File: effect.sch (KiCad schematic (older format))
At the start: 32 parts, among them Q1 2N7000, Q2 2N7000, U5 TL072, U6 TL072

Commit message: Fix a few values
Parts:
- removed C13: 47u, symbol Device:CP
- added C?: 47u, symbol Device:C
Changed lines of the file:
@@
-$EndComp
-$Comp
-L Device:CP C13
-U 1 1 60D39B10
-P 8650 1650
-F 0 "C13" H 8768 1696 50  0000 L CNN
-F 1 "47u" H 8768 1605 50  0000 L CNN
-F 2 "" H 8688 1500 50  0001 C CNN
-F 3 "~" H 8650 1650 50  0001 C CNN
-	1    8650 1650
-	1    0    0    -1
 $EndComp
 $Comp
@@
 Wire Wire Line
 	2400 1750 2400 2450
+$Comp
+L Device:C C?
+U 1 1 60E2FADA
+P 8650 1650
+F 0 "C?" H 8765 1696 50  0000 L CNN
+F 1 "47u" H 8765 1605 50  0000 L CNN
+F 2 "" H 8688 1500 50  0001 C CNN
+F 3 "~" H 8650 1650 50  0001 C CNN
+	1    8650 1650
+	1    0    0    -1
+$EndComp
 $EndSCHEMATC

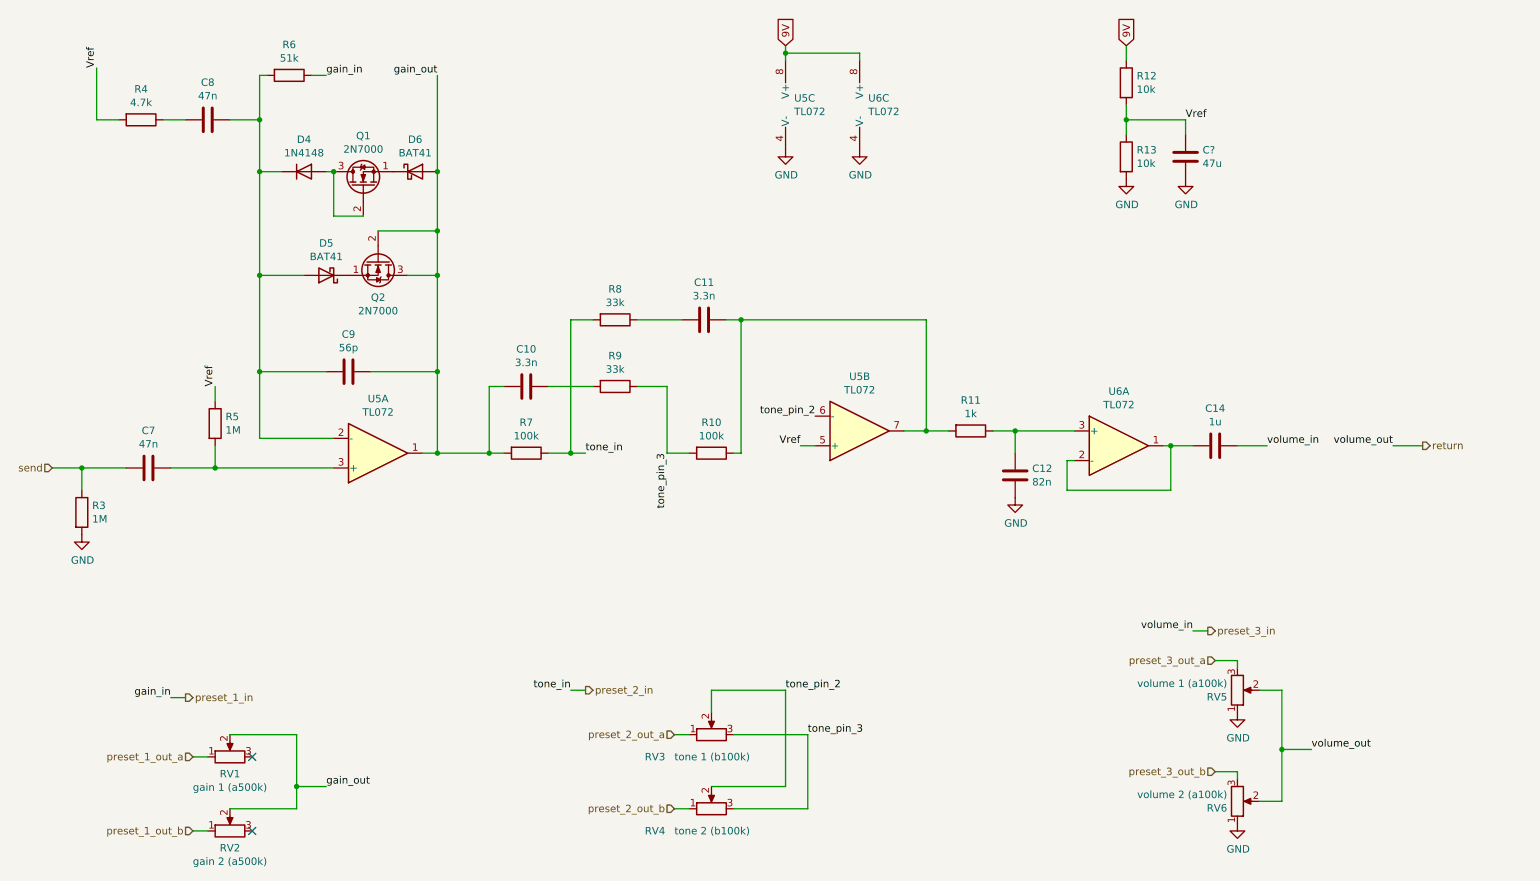
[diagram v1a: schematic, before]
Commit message: Now with an input buffer to preserve phase
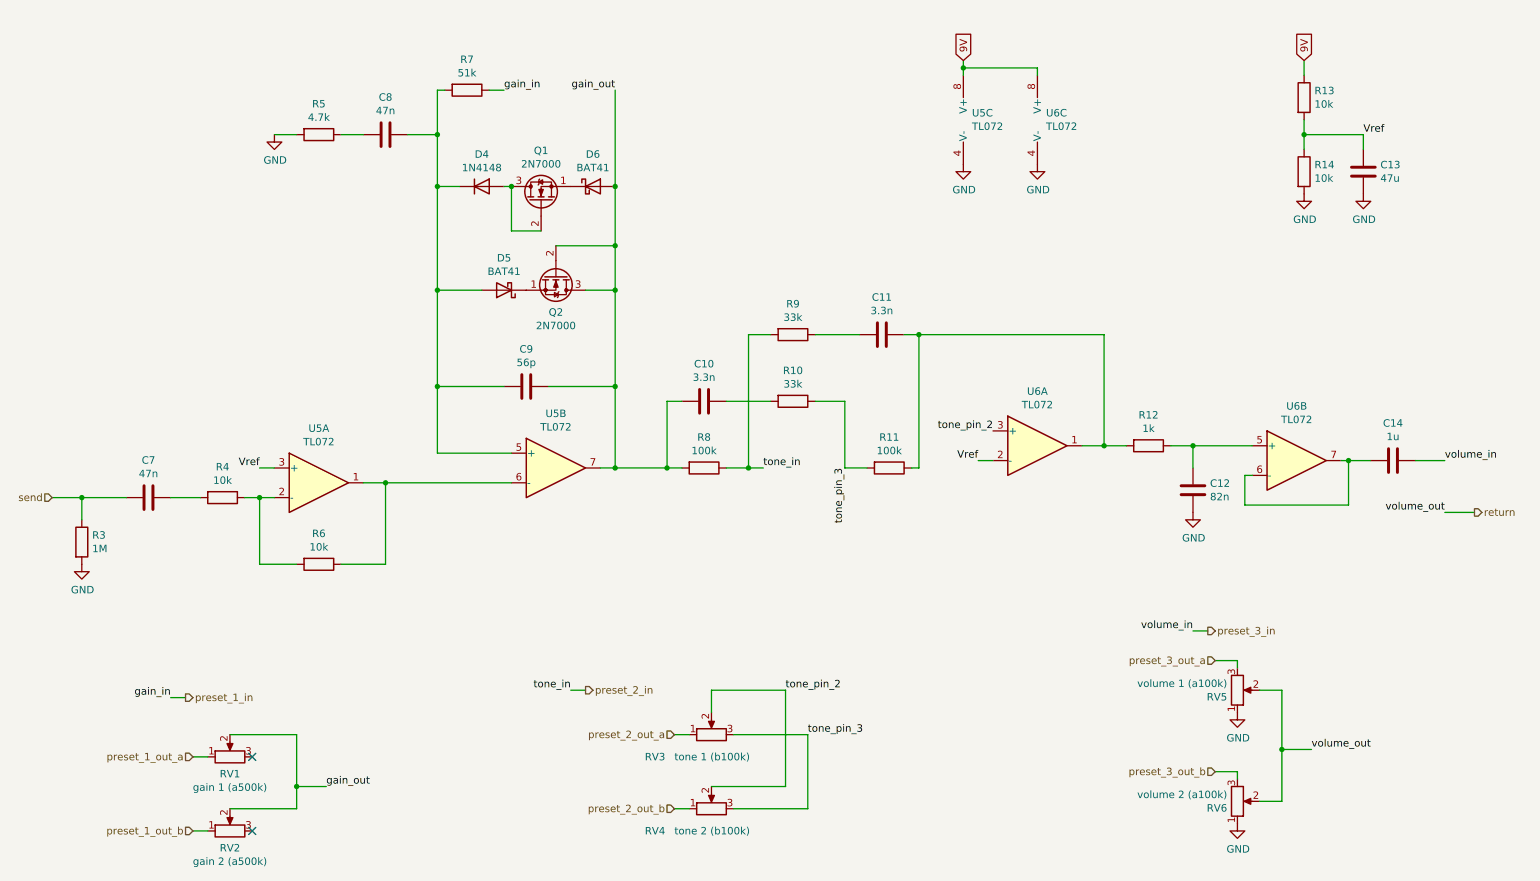
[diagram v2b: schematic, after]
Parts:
- removed R5: 1M, symbol Device:R
- added R4, R6: 10k, symbol Device:R
- added unit 2 of U6
- gave numbers to parts that had none: 1
- renumbered R9 to R10, R10 to R11, R11 to R12, R12 to R13, R13 to R14, R4 to R5, R6 to R7, R7 to R8, R8 to R9
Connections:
- net GND: now also R5.2
- net Vref: now also U5.3 (+), U6.2 (-); no longer R5.2, U5.5 (+)
- net gain_out: now also U5.7; no longer U5.1
- net tone_pin_2: now also U6.3 (+); no longer U5.6 (-)
- net at C8.1, C9.2, D4.1 (K)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: now also U5.5 (+); no longer U5.2 (-)
- net at C7.1: now also R4.2; no longer U5.3 (+)
- net at C11.1, R11.1, R12.2: now also U6.1; no longer U5.7
- net at C12.2, R12.1: now also U6.5 (+); no longer U6.3 (+)
- new net: C14.2, U6.6 (-), U6.7
- new net: R6.1, U5.1, U5.6 (-)
- new net: R4.1, R6.2, U5.2 (-)
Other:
- moved on the sheet: C10, C11, C12, C13, C14, C7, C8, C9, D4, D5, D6, Q1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

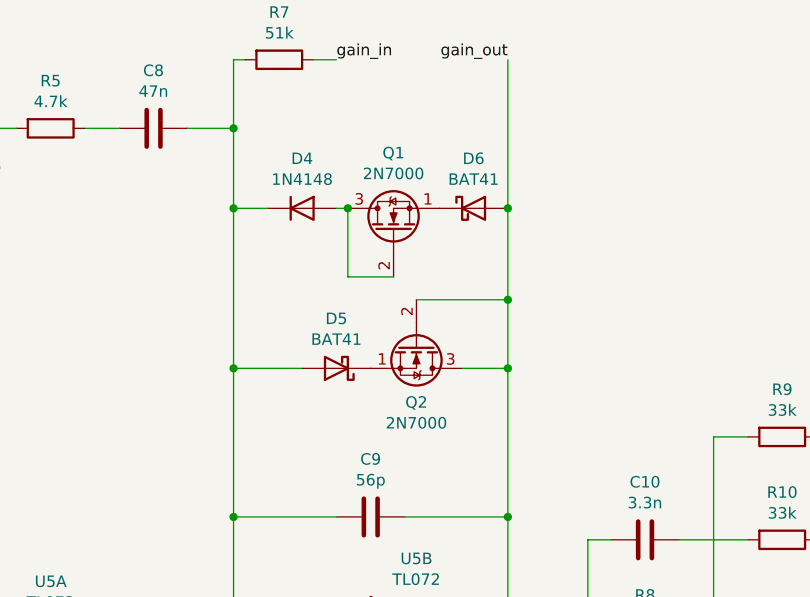
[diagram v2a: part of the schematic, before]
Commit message: Add resistor footprints/part numbers
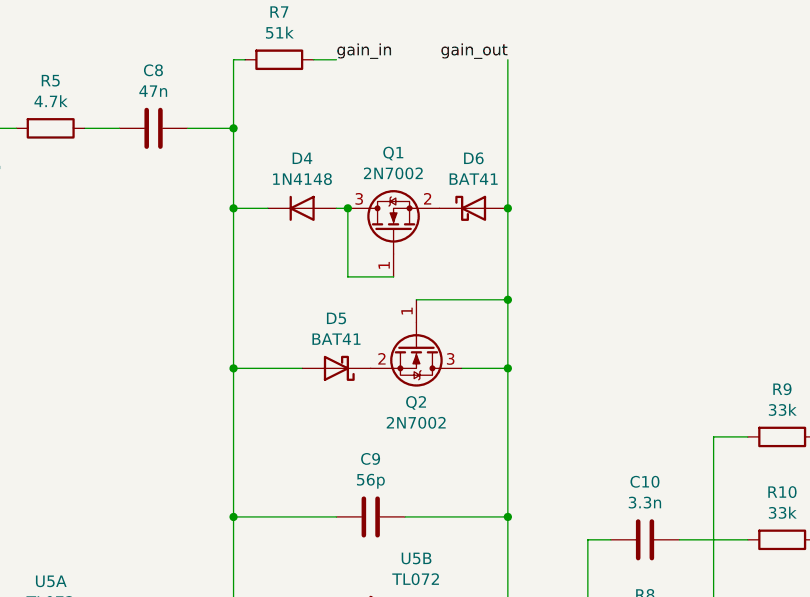
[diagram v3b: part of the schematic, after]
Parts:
- removed Q1, Q2: 2N7000, Package_TO_SOT_THT:TO-92_Inline, symbol Transistor_FET:2N7000
- added Q1, Q2: 2N7002, Package_TO_SOT_SMD:SOT-23, symbol Transistor_FET:2N7002
- R10, R9: footprint (none) -> Resistor_SMD:R_0603_1608Metric; LCSC (none) -> C4216
- R11, R8: footprint (none) -> Resistor_SMD:R_0603_1608Metric; LCSC (none) -> C25803
- R12: footprint (none) -> Resistor_SMD:R_0603_1608Metric; LCSC (none) -> C21190
- R13, R14, R4, R6: footprint (none) -> Resistor_SMD:R_0603_1608Metric; LCSC (none) -> C25804
- R3: footprint (none) -> Resistor_SMD:R_0603_1608Metric; LCSC (none) -> C22935
- R5: footprint (none) -> Resistor_SMD:R_0603_1608Metric; LCSC (none) -> C23162
- R7: footprint (none) -> Resistor_SMD:R_0603_1608Metric; LCSC (none) -> C23196
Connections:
- net gain_out: now also Q2.1 (G), Q2.3 (D)
- net at D5.1 (K): now also Q2.2 (S)
- net at D6.1 (K): now also Q1.2 (S)
- net at D4.2 (A): now also Q1.1 (G), Q1.3 (D)
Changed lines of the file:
@@
 F 0 "R7" V 3593 1200 50  0000 C CNN
 F 1 "51k" V 3684 1200 50  0000 C CNN
-F 2 "" V 3730 1200 50  0001 C CNN
+F 2 "Resistor_SMD:R_0603_1608Metric" V 3730 1200 50  0001 C CNN
 F 3 "~" H 3800 1200 50  0001 C CNN
+F 4 "C23196" V 3800 1200 50  0001 C CNN "LCSC"
 	1    3800 1200
 	0    1    1    0
@@
 F 0 "R5" V 2593 1500 50  0000 C CNN
 F 1 "4.7k" V 2684 1500 50  0000 C CNN
-F 2 "" V 2730 1500 50  0001 C CNN
+F 2 "Resistor_SMD:R_0603_1608Metric" V 2730 1500 50  0001 C CNN
 F 3 "~" H 2800 1500 50  0001 C CNN
+F 4 "C23162" V 2800 1500 50  0001 C CNN "LCSC"
 	1    2800 1500
 	0    1    1    0
@@
 F 0 "R3" H 1270 4296 50  0000 L CNN
 F 1 "1M" H 1270 4205 50  0000 L CNN
-F 2 "" V 1130 4250 50  0001 C CNN
+F 2 "Resistor_SMD:R_0603_1608Metric" V 1130 4250 50  0001 C CNN
 F 3 "~" H 1200 4250 50  0001 C CNN
+F 4 "C22935" H 1200 4250 50  0001 C CNN "LCSC"
 	1    1200 4250
 	1    0    0    -1
@@
 F 0 "R8" V 5193 3750 50  0000 C CNN
 F 1 "100k" V 5284 3750 50  0000 C CNN
-F 2 "" V 5330 3750 50  0001 C CNN
+F 2 "Resistor_SMD:R_0603_1608Metric" V 5330 3750 50  0001 C CNN
 F 3 "~" H 5400 3750 50  0001 C CNN
+F 4 "C25803" V 5400 3750 50  0001 C CNN "LCSC"
 	1    5400 3750
 	0    1    1    0
@@
 F 0 "R10" V 5793 3300 50  0000 C CNN
 F 1 "33k" V 5884 3300 50  0000 C CNN
-F 2 "" V 5930 3300 50  0001 C CNN
+F 2 "Resistor_SMD:R_0603_1608Metric" V 5930 3300 50  0001 C CNN
 F 3 "~" H 6000 3300 50  0001 C CNN
+F 4 "C4216" V 6000 3300 50  0001 C CNN "LCSC"
 	1    6000 3300
 	0    1    1    0
@@
 F 0 "R9" V 5793 2850 50  0000 C CNN
 F 1 "33k" V 5884 2850 50  0000 C CNN
-F 2 "" V 5930 2850 50  0001 C CNN
+F 2 "Resistor_SMD:R_0603_1608Metric" V 5930 2850 50  0001 C CNN
 F 3 "~" H 6000 2850 50  0001 C CNN
+F 4 "C4216" V 6000 2850 50  0001 C CNN "LCSC"
 	1    6000 2850
 	0    1    1    0
@@
 F 0 "R11" V 6443 3750 50  0000 C CNN
 F 1 "100k" V 6534 3750 50  0000 C CNN
-F 2 "" V 6580 3750 50  0001 C CNN
+F 2 "Resistor_SMD:R_0603_1608Metric" V 6580 3750 50  0001 C CNN
 F 3 "~" H 6650 3750 50  0001 C CNN
+F 4 "C25803" V 6650 3750 50  0001 C CNN "LCSC"
 	1    6650 3750
 	0    1    1    0
@@
 F 0 "R12" V 8193 3600 50  0000 C CNN
 F 1 "1k" V 8284 3600 50  0000 C CNN
-F 2 "" V 8330 3600 50  0001 C CNN
+F 2 "Resistor_SMD:R_0603_1608Metric" V 8330 3600 50  0001 C CNN
 F 3 "~" H 8400 3600 50  0001 C CNN
+F 4 "C21190" V 8400 3600 50  0001 C CNN "LCSC"
 	1    8400 3600
 	0    1    1    0
@@
 F 0 "R13" H 9520 1296 50  0000 L CNN
 F 1 "10k" H 9520 1205 50  0000 L CNN
-F 2 "" V 9380 1250 50  0001 C CNN
+F 2 "Resistor_SMD:R_0603_1608Metric" V 9380 1250 50  0001 C CNN
 F 3 "~" H 9450 1250 50  0001 C CNN
+F 4 "C25804" H 9450 1250 50  0001 C CNN "LCSC"
 	1    9450 1250
 	1    0    0    -1
@@
 F 0 "R14" H 9520 1796 50  0000 L CNN
 F 1 "10k" H 9520 1705 50  0000 L CNN
-F 2 "" V 9380 1750 50  0001 C CNN
+F 2 "Resistor_SMD:R_0603_1608Metric" V 9380 1750 50  0001 C CNN
 F 3 "~" H 9450 1750 50  0001 C CNN
+F 4 "C25804" H 9450 1750 50  0001 C CNN "LCSC"
 	1    9450 1750
 	1    0    0    -1
@@
 Wire Wire Line
 	9450 1500 9850 1500
-$Comp
-L Transistor_FET:2N7000 Q2
-U 1 1 60D90FC1
-P 4400 2450
-F 0 "Q2" V 4649 2450 50  0000 C CNN
-F 1 "2N7000" V 4740 2450 50  0000 C CNN
-F 2 "Package_TO_SOT_THT:TO-92_Inline" H 4600 2375 50  0001 L CIN
-F 3 "https://www.onsemi.com/pub/Collateral/NDS7002A-D.PDF" H 4400 2450 50  0001 L CNN
-	1    4400 2450
-	0    1    1    0
-$EndComp
 $Comp
 L Diode:BAT41 D5
@@
 	-1   0    0    1
 $EndComp
-$Comp
-L Transistor_FET:2N7000 Q1
-U 1 1 60D9C1B6
-P 4300 1950
-F 0 "Q1" V 4642 1950 50  0000 C CNN
-F 1 "2N7000" V 4551 1950 50  0000 C CNN
-F 2 "Package_TO_SOT_THT:TO-92_Inline" H 4500 1875 50  0001 L CIN
-F 3 "https://www.onsemi.com/pub/Collateral/NDS7002A-D.PDF" H 4300 1950 50  0001 L CNN
-	1    4300 1950
-	0    -1   -1   0
-$EndComp
 Wire Wire Line
 	4300 2150 4100 2150
@@
 Wire Wire Line
 	4050 1850 4100 1850
-Connection ~ 4100 1850
 $Comp
 L Diode:1N4148 D4
@@
 F 0 "R4" V 1943 3950 50  0000 C CNN
 F 1 "10k" V 2034 3950 50  0000 C CNN
-F 2 "" V 2080 3950 50  0001 C CNN
+F 2 "Resistor_SMD:R_0603_1608Metric" V 2080 3950 50  0001 C CNN
 F 3 "~" H 2150 3950 50  0001 C CNN
+F 4 "C25804" V 2150 3950 50  0001 C CNN "LCSC"
 	1    2150 3950
 	0    1    1    0
@@
 F 0 "R6" V 2593 4400 50  0000 C CNN
 F 1 "10k" V 2684 4400 50  0000 C CNN
-F 2 "" V 2730 4400 50  0001 C CNN
+F 2 "Resistor_SMD:R_0603_1608Metric" V 2730 4400 50  0001 C CNN
 F 3 "~" H 2800 4400 50  0001 C CNN
+F 4 "C25804" V 2800 4400 50  0001 C CNN "LCSC"
 	1    2800 4400
 	0    1    1    0
@@
 Wire Wire Line
 	2400 3750 2500 3750
+$Comp
+L Transistor_FET:2N7002 Q1
+U 1 1 60ED8C47
+P 4300 1950
+F 0 "Q1" V 4642 1950 50  0000 C CNN
+F 1 "2N7002" V 4551 1950 50  0000 C CNN
+F 2 "Package_TO_SOT_SMD:SOT-23" H 4500 1875 50  0001 L CIN
+F 3 "https://www.onsemi.com/pub/Collateral/NDS7002A-D.PDF" H 4300 1950 50  0001 L CNN
+	1    4300 1950
+	0    -1   -1   0
+$EndComp
+Connection ~ 4100 1850
+$Comp
+L Transistor_FET:2N7002 Q2
+U 1 1 60EDE1F5
+P 4400 2450
+F 0 "Q2" V 4649 2450 50  0000 C CNN
+F 1 "2N7002" V 4740 2450 50  0000 C CNN
+F 2 "Package_TO_SOT_SMD:SOT-23" H 4600 2375 50  0001 L CIN
+F 3 "https://www.onsemi.com/pub/Collateral/NDS7002A-D.PDF" H 4400 2450 50  0001 L CNN
+	1    4400 2450
+	0    1    1    0
+$EndComp
 $EndSCHEMATC

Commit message: Capacitors
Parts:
- C10, C11: footprint (none) -> Capacitor_SMD:C_0603_1608Metric; LCSC (none) -> C1613
- C12: value 82n -> 47n; footprint (none) -> Capacitor_SMD:C_0603_1608Metric; LCSC (none) -> C1622
- C13: footprint (none) -> Capacitor_SMD:C_1206_3216Metric; LCSC (none) -> C96123
- C14: footprint (none) -> Capacitor_SMD:C_0603_1608Metric; LCSC (none) -> C15849
- C7, C8: footprint (none) -> Capacitor_SMD:C_0603_1608Metric; LCSC (none) -> C1622
- C9: footprint (none) -> Capacitor_SMD:C_0603_1608Metric; LCSC (none) -> C39148
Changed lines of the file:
@@
 F 0 "C7" V 1398 3950 50  0000 C CNN
 F 1 "47n" V 1489 3950 50  0000 C CNN
-F 2 "" H 1688 3800 50  0001 C CNN
+F 2 "Capacitor_SMD:C_0603_1608Metric" H 1688 3800 50  0001 C CNN
 F 3 "~" H 1650 3950 50  0001 C CNN
+F 4 "C1622" V 1650 3950 50  0001 C CNN "LCSC"
 	1    1650 3950
 	0    1    1    0
@@
 F 0 "C8" V 2998 1500 50  0000 C CNN
 F 1 "47n" V 3089 1500 50  0000 C CNN
-F 2 "" H 3288 1350 50  0001 C CNN
+F 2 "Capacitor_SMD:C_0603_1608Metric" H 3288 1350 50  0001 C CNN
 F 3 "~" H 3250 1500 50  0001 C CNN
+F 4 "C1622" V 3250 1500 50  0001 C CNN "LCSC"
 	1    3250 1500
 	0    1    1    0
@@
 F 0 "C9" V 3948 3200 50  0000 C CNN
 F 1 "56p" V 4039 3200 50  0000 C CNN
-F 2 "" H 4238 3050 50  0001 C CNN
+F 2 "Capacitor_SMD:C_0603_1608Metric" H 4238 3050 50  0001 C CNN
 F 3 "~" H 4200 3200 50  0001 C CNN
+F 4 "C39148" V 4200 3200 50  0001 C CNN "LCSC"
 	1    4200 3200
 	0    1    1    0
@@
 F 0 "C10" V 5148 3300 50  0000 C CNN
 F 1 "3.3n" V 5239 3300 50  0000 C CNN
-F 2 "" H 5438 3150 50  0001 C CNN
+F 2 "Capacitor_SMD:C_0603_1608Metric" H 5438 3150 50  0001 C CNN
 F 3 "~" H 5400 3300 50  0001 C CNN
+F 4 "C1613" V 5400 3300 50  0001 C CNN "LCSC"
 	1    5400 3300
 	0    1    1    0
@@
 F 0 "C11" V 6348 2850 50  0000 C CNN
 F 1 "3.3n" V 6439 2850 50  0000 C CNN
-F 2 "" H 6638 2700 50  0001 C CNN
+F 2 "Capacitor_SMD:C_0603_1608Metric" H 6638 2700 50  0001 C CNN
 F 3 "~" H 6600 2850 50  0001 C CNN
+F 4 "C1613" V 6600 2850 50  0001 C CNN "LCSC"
 	1    6600 2850
 	0    1    1    0
@@
 P 8700 3900
 F 0 "C12" H 8585 3854 50  0000 R CNN
-F 1 "82n" H 8585 3945 50  0000 R CNN
-F 2 "" H 8738 3750 50  0001 C CNN
+F 1 "47n" H 8585 3945 50  0000 R CNN
+F 2 "Capacitor_SMD:C_0603_1608Metric" H 8738 3750 50  0001 C CNN
 F 3 "~" H 8700 3900 50  0001 C CNN
+F 4 "C1622" H 8700 3900 50  0001 C CNN "LCSC"
 	1    8700 3900
 	-1   0    0    1
@@
 F 0 "C14" V 9798 3700 50  0000 C CNN
 F 1 "1u" V 9889 3700 50  0000 C CNN
-F 2 "" H 10088 3550 50  0001 C CNN
+F 2 "Capacitor_SMD:C_0603_1608Metric" H 10088 3550 50  0001 C CNN
 F 3 "~" H 10050 3700 50  0001 C CNN
+F 4 "C15849" V 10050 3700 50  0001 C CNN "LCSC"
 	1    10050 3700
 	0    1    1    0
@@
 F 0 "C13" H 9965 1796 50  0000 L CNN
 F 1 "47u" H 9965 1705 50  0000 L CNN
-F 2 "" H 9888 1600 50  0001 C CNN
+F 2 "Capacitor_SMD:C_1206_3216Metric" H 9888 1600 50  0001 C CNN
 F 3 "~" H 9850 1750 50  0001 C CNN
+F 4 "C96123" H 9850 1750 50  0001 C CNN "LCSC"
 	1    9850 1750
 	1    0    0    -1

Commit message: Everything except those damn pots
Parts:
- removed D4: 1N4148, Diode_THT:D_DO-35_SOD27_P7.62mm_Horizontal, symbol Diode:1N4148
- added D4: 1N4148W, Diode_SMD:D_SOD-123, symbol Diode:1N4148W
- Q1, Q2: LCSC (none) -> C8545
- U5, U6: footprint (none) -> Package_SO:SOIC-8_3.9x4.9mm_P1.27mm; LCSC (none) -> C6961
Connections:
- net at C8.1, C9.2, D5.2 (A)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: now also D4.1 (K)
- net at Q1.1 (G), Q1.3 (D): now also D4.2 (A)
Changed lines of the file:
@@
 F 0 "U6" H 7650 3967 50  0000 C CNN
 F 1 "TL072" H 7650 3876 50  0000 C CNN
-F 2 "" H 7650 3600 50  0001 C CNN
+F 2 "Package_SO:SOIC-8_3.9x4.9mm_P1.27mm" H 7650 3600 50  0001 C CNN
 F 3 "http://www.ti.com/lit/ds/symlink/tl071.pdf" H 7650 3600 50  0001 C CNN
+F 4 "C6961" H 7650 3600 50  0001 C CNN "LCSC"
 	1    7650 3600
 	1    0    0    -1
@@
 F 0 "U5" H 7208 1446 50  0000 L CNN
 F 1 "TL072" H 7208 1355 50  0000 L CNN
-F 2 "" H 7250 1400 50  0001 C CNN
+F 2 "Package_SO:SOIC-8_3.9x4.9mm_P1.27mm" H 7250 1400 50  0001 C CNN
 F 3 "http://www.ti.com/lit/ds/symlink/tl071.pdf" H 7250 1400 50  0001 C CNN
+F 4 "C6961" H 7250 1400 50  0001 C CNN "LCSC"
 	3    7250 1400
 	1    0    0    -1
@@
 F 0 "U6" H 7708 1446 50  0000 L CNN
 F 1 "TL072" H 7708 1355 50  0000 L CNN
-F 2 "" H 7750 1400 50  0001 C CNN
+F 2 "Package_SO:SOIC-8_3.9x4.9mm_P1.27mm" H 7750 1400 50  0001 C CNN
 F 3 "http://www.ti.com/lit/ds/symlink/tl071.pdf" H 7750 1400 50  0001 C CNN
+F 4 "C6961" H 7750 1400 50  0001 C CNN "LCSC"
 	3    7750 1400
 	1    0    0    -1
@@
 Wire Wire Line
 	4050 1850 4100 1850
-$Comp
-L Diode:1N4148 D4
-U 1 1 60DB901B
-P 3900 1850
-F 0 "D4" H 3900 2067 50  0000 C CNN
-F 1 "1N4148" H 3900 1976 50  0000 C CNN
-F 2 "Diode_THT:D_DO-35_SOD27_P7.62mm_Horizontal" H 3900 1675 50  0001 C CNN
-F 3 "https://assets.nexperia.com/documents/data-sheet/1N4148_1N4448.pdf" H 3900 1850 50  0001 C CNN
-	1    3900 1850
-	1    0    0    -1
-$EndComp
 Wire Wire Line
 	4800 2550 4800 3200
@@
 F 0 "U5" H 2800 4217 50  0000 C CNN
 F 1 "TL072" H 2800 4126 50  0000 C CNN
-F 2 "" H 2800 3850 50  0001 C CNN
+F 2 "Package_SO:SOIC-8_3.9x4.9mm_P1.27mm" H 2800 3850 50  0001 C CNN
 F 3 "http://www.ti.com/lit/ds/symlink/tl071.pdf" H 2800 3850 50  0001 C CNN
+F 4 "C6961" H 2800 3850 50  0001 C CNN "LCSC"
 	1    2800 3850
 	1    0    0    -1
@@
 F 0 "U5" H 4400 4117 50  0000 C CNN
 F 1 "TL072" H 4400 4026 50  0000 C CNN
-F 2 "" H 4400 3750 50  0001 C CNN
+F 2 "Package_SO:SOIC-8_3.9x4.9mm_P1.27mm" H 4400 3750 50  0001 C CNN
 F 3 "http://www.ti.com/lit/ds/symlink/tl071.pdf" H 4400 3750 50  0001 C CNN
+F 4 "C6961" H 4400 3750 50  0001 C CNN "LCSC"
 	2    4400 3750
 	1    0    0    -1
@@
 F 0 "U6" H 9400 4067 50  0000 C CNN
 F 1 "TL072" H 9400 3976 50  0000 C CNN
-F 2 "" H 9400 3700 50  0001 C CNN
+F 2 "Package_SO:SOIC-8_3.9x4.9mm_P1.27mm" H 9400 3700 50  0001 C CNN
 F 3 "http://www.ti.com/lit/ds/symlink/tl071.pdf" H 9400 3700 50  0001 C CNN
+F 4 "C6961" H 9400 3700 50  0001 C CNN "LCSC"
 	2    9400 3700
 	1    0    0    -1
@@
 F 2 "Package_TO_SOT_SMD:SOT-23" H 4500 1875 50  0001 L CIN
 F 3 "https://www.onsemi.com/pub/Collateral/NDS7002A-D.PDF" H 4300 1950 50  0001 L CNN
+F 4 "C8545" V 4300 1950 50  0001 C CNN "LCSC"
 	1    4300 1950
 	0    -1   -1   0
@@
 F 2 "Package_TO_SOT_SMD:SOT-23" H 4600 2375 50  0001 L CIN
 F 3 "https://www.onsemi.com/pub/Collateral/NDS7002A-D.PDF" H 4400 2450 50  0001 L CNN
+F 4 "C8545" V 4400 2450 50  0001 C CNN "LCSC"
 	1    4400 2450
 	0    1    1    0
 $EndComp
+$Comp
+L Diode:1N4148W D4
+U 1 1 60FC72F8
+P 3900 1850
+F 0 "D4" H 3900 2067 50  0000 C CNN
+F 1 "1N4148W" H 3900 1976 50  0000 C CNN
+F 2 "Diode_SMD:D_SOD-123" H 3900 1675 50  0001 C CNN
+F 3 "https://www.vishay.com/docs/85748/1n4148w.pdf" H 3900 1850 50  0001 C CNN
+F 4 "C81598" H 3900 1850 50  0001 C CNN "LCSC"
+	1    3900 1850
+	1    0    0    -1
+$EndComp
 $EndSCHEMATC
